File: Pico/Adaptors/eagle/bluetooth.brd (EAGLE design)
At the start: 23.8 x 17.8 mm, 4 parts, among them U1 HC_05

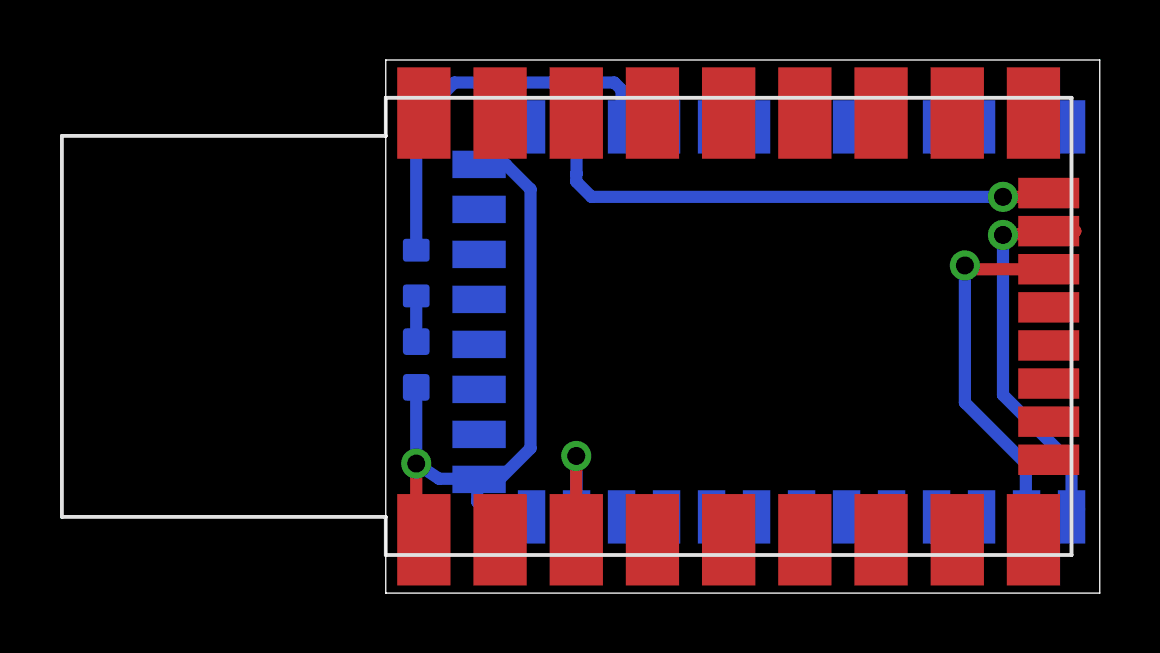
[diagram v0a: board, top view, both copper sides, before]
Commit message: nrf24 adaptor, and DRC
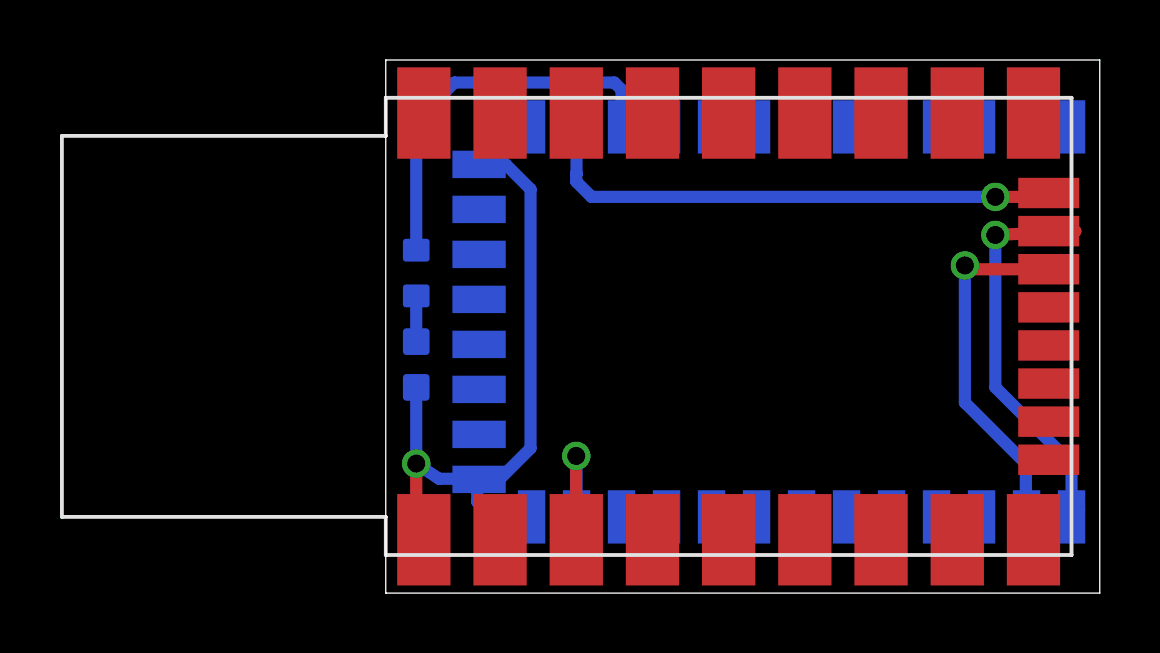
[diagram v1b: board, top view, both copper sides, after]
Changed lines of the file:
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@@
 </class>
 </classes>
-<designrules name="default">
+<designrules name="oshpark-2layer">
 <description language="de">&lt;b&gt;EAGLE Design Rules&lt;/b&gt;
 &lt;p&gt;
@@
 Einstellungen hier und speichern die Design Rules unter
 einem neuen Namen ab.</description>
-<description language="en">&lt;b&gt;EAGLE Design Rules&lt;/b&gt;
+<description language="en">&lt;b&gt;Laen's PCB Order Design Rules&lt;/b&gt;
 &lt;p&gt;
-The default Design Rules have been set to cover
-a wide range of applications. Your particular design
-may have different requirements, so please make the
-necessary adjustments and save your customized
-design rules under a new name.</description>
+Please make sure your boards conform to these design rules.</description>
 <param name="layerSetup" value="(1*16)"/>
-<param name="mtCopper" value="0.035mm 0.035mm 0.035mm 0.035mm 0.035mm 0.035mm 0.035mm 0.035mm 0.035mm 0.035mm 0.035mm 0.035mm 0.035mm 0.035mm 0.035mm 0.035mm"/>
-<param name="mtIsolate" value="1.5mm 0.15mm 0.2mm 0.15mm 0.2mm 0.15mm 0.2mm 0.15mm 0.2mm 0.15mm 0.2mm 0.15mm 0.2mm 0.15mm 0.2mm"/>
-<param name="mdWireWire" value="8mil"/>
-<param name="mdWirePad" value="8mil"/>
-<param name="mdWireVia" value="8mil"/>
-<param name="mdPadPad" value="8mil"/>
-<param name="mdPadVia" value="8mil"/>
-<param name="mdViaVia" value="8mil"/>
-<param name="mdSmdPad" value="8mil"/>
-<param name="mdSmdVia" value="8mil"/>
-<param name="mdSmdSmd" value="8mil"/>
+<param name="mtCopper" value="0.0356mm 0.0356mm 0.0356mm 0.0356mm 0.0356mm 0.0356mm 0.0356mm 0.0356mm 0.0356mm 0.0356mm 0.0356mm 0.0356mm 0.0356mm 0.0356mm 0.0356mm 0.0356mm"/>
+<param name="mtIsolate" value="1.5011mm 0.1499mm 0.2007mm 0.1499mm 0.2007mm 0.1499mm 0.2007mm 0.1499mm 0.2007mm 0.1499mm 0.2007mm 0.1499mm 0.2007mm 0.1499mm 0.2007mm"/>
+<param name="mdWireWire" value="6mil"/>
+<param name="mdWirePad" value="6mil"/>
+<param name="mdWireVia" value="6mil"/>
+<param name="mdPadPad" value="6mil"/>
+<param name="mdPadVia" value="6mil"/>
+<param name="mdViaVia" value="6mil"/>
+<param name="mdSmdPad" value="6mil"/>
+<param name="mdSmdVia" value="6mil"/>
+<param name="mdSmdSmd" value="6mil"/>
 <param name="mdViaViaSameLayer" value="8mil"/>
 <param name="mnLayersViaInSmd" value="2"/>
-<param name="mdCopperDimension" value="40mil"/>
-<param name="mdDrill" value="8mil"/>
+<param name="mdCopperDimension" value="15mil"/>
+<param name="mdDrill" value="6mil"/>
 <param name="mdSmdStop" value="0mil"/>
-<param name="msWidth" value="10mil"/>
-<param name="msDrill" value="24mil"/>
-<param name="msMicroVia" value="9.99mm"/>
+<param name="msWidth" value="6mil"/>
+<param name="msDrill" value="13mil"/>
+<param name="msMicroVia" value="13mil"/>
 <param name="msBlindViaRatio" value="0.5"/>
 <param name="rvPadTop" value="0.25"/>
@@
 <param name="rvMicroViaOuter" value="0.25"/>
 <param name="rvMicroViaInner" value="0.25"/>
-<param name="rlMinPadTop" value="10mil"/>
+<param name="rlMinPadTop" value="7mil"/>
 <param name="rlMaxPadTop" value="20mil"/>
-<param name="rlMinPadInner" value="10mil"/>
+<param name="rlMinPadInner" value="7mil"/>
 <param name="rlMaxPadInner" value="20mil"/>
-<param name="rlMinPadBottom" value="10mil"/>
+<param name="rlMinPadBottom" value="7mil"/>
 <param name="rlMaxPadBottom" value="20mil"/>
-<param name="rlMinViaOuter" value="8mil"/>
+<param name="rlMinViaOuter" value="7mil"/>
 <param name="rlMaxViaOuter" value="20mil"/>
-<param name="rlMinViaInner" value="8mil"/>
+<param name="rlMinViaInner" value="7mil"/>
 <param name="rlMaxViaInner" value="20mil"/>
 <param name="rlMinMicroViaOuter" value="4mil"/>
@@
 <contactref element="U$1" pad="A3"/>
 <wire x1="22.098" y1="12.065" x2="22.987" y2="12.065" width="0.4064" layer="1"/>
-<wire x1="22.987" y1="12.065" x2="20.574" y2="11.938" width="0.4064" layer="1"/>
-<via x="20.574" y="11.938" extent="1-16" drill="0.6" shape="octagon"/>
+<wire x1="22.987" y1="12.065" x2="20.32" y2="11.938" width="0.4064" layer="1"/>
+<via x="20.32" y="11.938" extent="1-16" drill="0.6" shape="octagon"/>
 <wire x1="23.114" y1="2.794" x2="22.86" y2="2.54" width="0.4064" layer="16"/>
-<wire x1="20.574" y1="11.938" x2="20.574" y2="6.604" width="0.4064" layer="16"/>
-<wire x1="20.574" y1="6.604" x2="22.86" y2="4.318" width="0.4064" layer="16"/>
+<wire x1="20.32" y1="11.938" x2="20.32" y2="6.858" width="0.4064" layer="16"/>
+<wire x1="20.32" y1="6.858" x2="22.86" y2="4.318" width="0.4064" layer="16"/>
 <wire x1="22.86" y1="4.318" x2="22.86" y2="2.54" width="0.4064" layer="16"/>
 </signal>
@@
 <wire x1="6.35" y1="13.97" x2="6.35" y2="13.716" width="0.4064" layer="16"/>
 <wire x1="6.35" y1="13.716" x2="6.858" y2="13.208" width="0.4064" layer="16"/>
-<wire x1="6.858" y1="13.208" x2="20.574" y2="13.208" width="0.4064" layer="16"/>
-<via x="20.574" y="13.208" extent="1-16" drill="0.6" shape="octagon"/>
-<wire x1="20.574" y1="13.208" x2="22.225" y2="13.208" width="0.4064" layer="1"/>
+<wire x1="6.858" y1="13.208" x2="20.32" y2="13.208" width="0.4064" layer="16"/>
+<via x="20.32" y="13.208" extent="1-16" drill="0.6" shape="octagon"/>
+<wire x1="20.32" y1="13.208" x2="22.225" y2="13.208" width="0.4064" layer="1"/>
 <wire x1="22.225" y1="13.208" x2="22.098" y2="13.335" width="0.4064" layer="1"/>
 </signal>
